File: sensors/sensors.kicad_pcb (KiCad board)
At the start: 2 copper layers, 73 x 56 mm, 84 parts, among them J1 GPIO, J2 JP_CAN, J3 JP_PWM, J4 JP_ADC, J5 JP_GPS, J6 JP_RADIO, SW1 SW_SPDT_321, SW2 SW_SPDT_321, U1 SC16IS752IPW, U2 PCA9685PW, U3 ICM-42605, U4 IST8310, U5 MS5611-01BA, U6 74LVC1G86, U7 ADS1115IDGS, U8 MCP2515-xST, U9 MCP2562-E-MF, Y2 25M-3225, Y4 16MHz

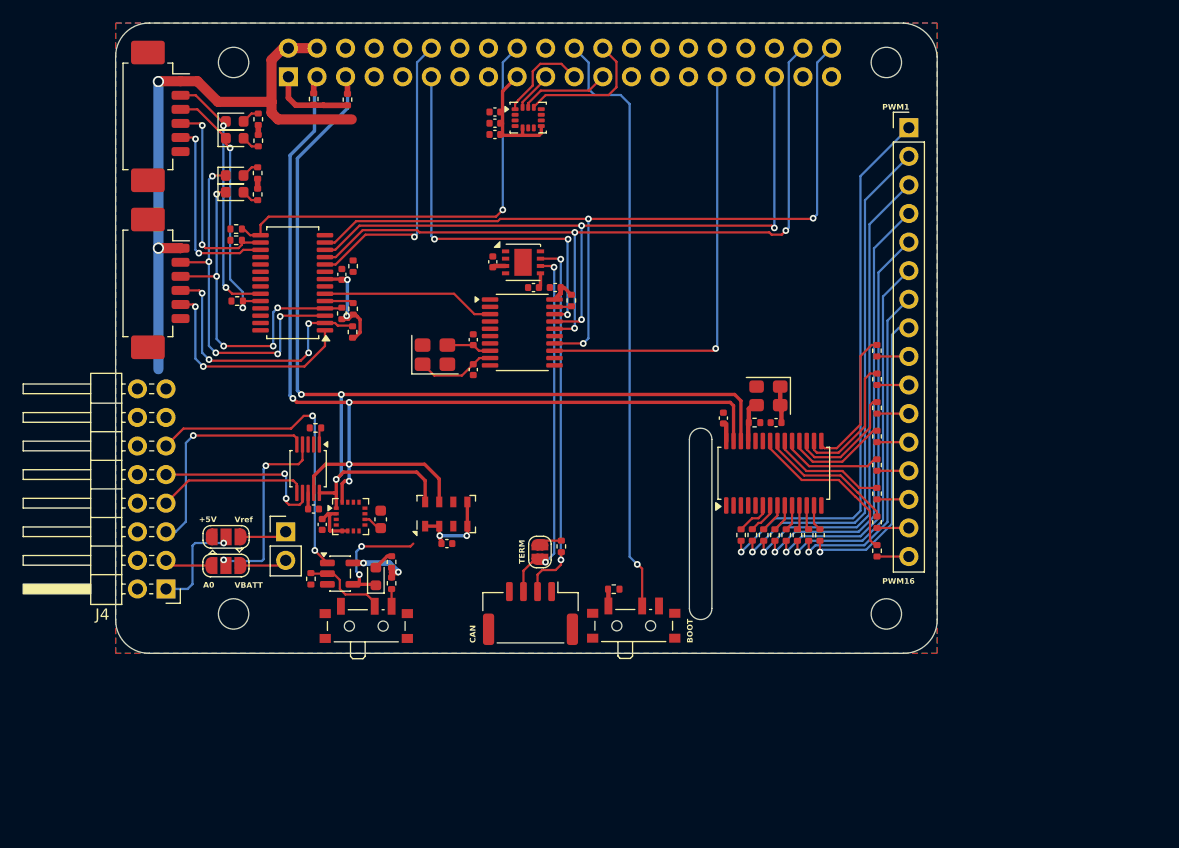
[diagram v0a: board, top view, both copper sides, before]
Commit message: changes from dshot branch
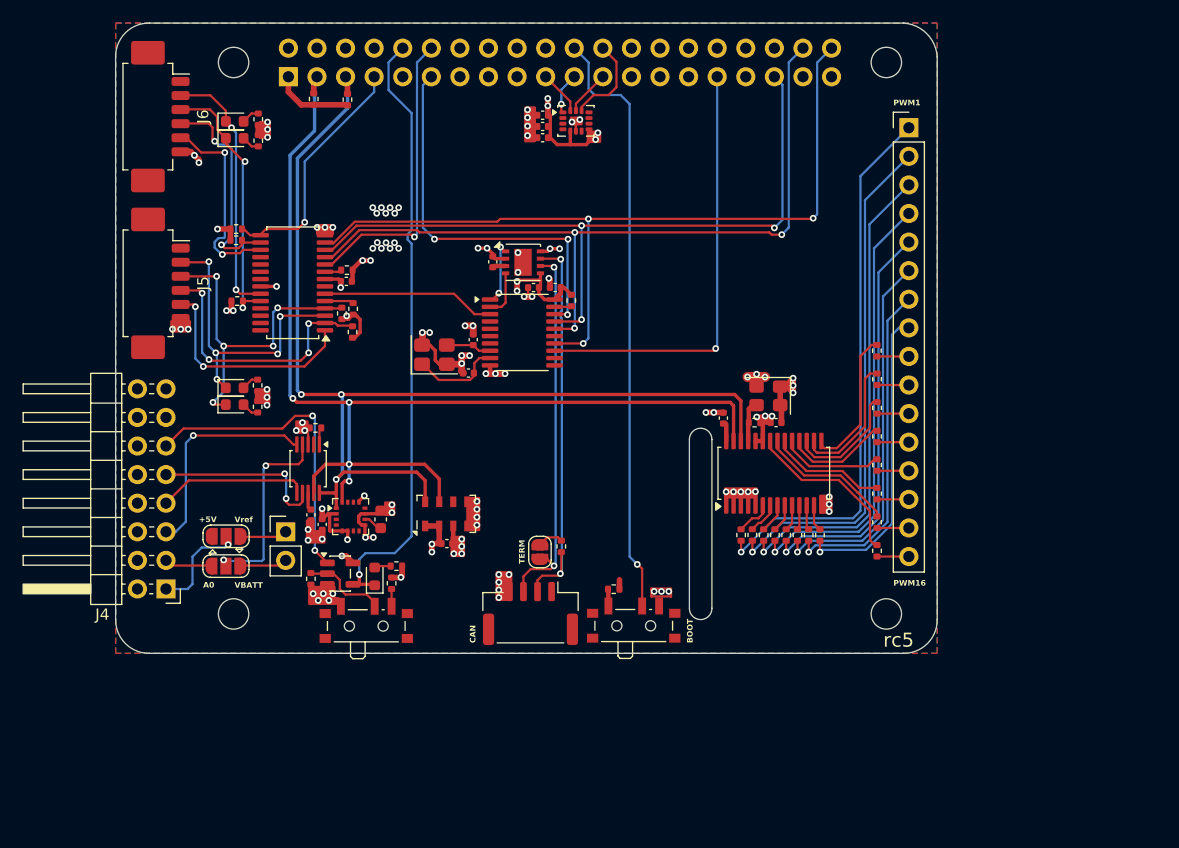
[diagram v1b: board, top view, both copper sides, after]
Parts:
- moved D1 18.9 mm to (110.6, 76.4)
- moved D2 18.9 mm to (110.6, 77.9)
- moved R6 18.9 mm to (112.6, 76.2)
- moved R8 18.9 mm to (112.6, 78.1)
- moved C6 4.25 mm to (137.9, 52.2)
- moved C7 4.25 mm to (137.9, 54.2)
- moved C8 4.25 mm to (137.9, 53.2)
- moved U3 4.25 mm to (140.9, 52.7)
- moved C1 0.74 mm to (120.5, 67.0), turned to 0 degrees
- moved R3 0.65 mm to (120.5, 66.0), turned to 0 degrees
- moved C12 0.57 mm to (117.3, 87.7), turned to -90 degrees
- moved R31 0.57 mm to (125.0, 92.2), turned to 180 degrees
- moved C13 0.52 mm to (131.3, 75.1), turned to 0 degrees
- moved D5 0.10 mm to (123.0, 93.2)
- moved JP1 0.05 mm to (109.8, 89.6)
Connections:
- net /ID_SCL renamed /GPIO1/SCL0
- net /ID_SDA renamed /GPIO0/SDA0
- R2 pad 2: /SDIODAT0/GPIO24 -> /GPIO4/GPCLK0
- U1 pad 15: /SDIODAT0/GPIO24 -> /GPIO4/GPCLK0
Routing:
- net +5V: track 59.0 -> 4.94 mm, vias 2 -> 14
- net GND: track 0.00 -> 47.5 mm, vias 0 -> 79
- net /GPIO15/RXD0: track 10.9 -> 55.3 mm, vias 2 -> 1
- net /SDIODAT0/GPIO24: track 39.8 -> 0.00 mm, vias 1 -> 0
- net /GPIO4/GPCLK0: track 0.00 -> 21.8 mm, vias 0 -> 1
- net +3V3: track 54.3 -> 60.6 mm, vias 6 -> 31
- net /CAN/TXCAN: track 0.00 -> 5.78 mm, vias 0 -> 2
- net /UART/TXA: track 32.8 -> 27.4 mm
- net /GPIO9/SPI0.MISO: track 8.45 -> 3.70 mm, vias 0 -> 1
- net /CAN/RXCAN: track 0.00 -> 4.15 mm
- net /GPIO11/SPI0.SCLK: track 7.97 -> 4.00 mm
- net /GPIO8/SPI0.CE0: track 12.0 -> 8.11 mm
- net /CAN/CANL: track 31.9 -> 33.9 mm
- net /UART/RXA: track 31.5 -> 29.9 mm
- net /CAN/CANH: track 33.6 -> 35.2 mm
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- added copper zone on B.Cu, net +3V3
- added copper zone on F.Cu, net +5V
- added copper zone on In1.Cu, net GND
- added copper zone on In2.Cu, net GND
- removed copper zone on B.Cu, net GND
- removed copper zone on F.Cu, net GND
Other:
- copper layers 2 -> 4
- board text added: "rc5"

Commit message: added 74ACT595 SIPO for DShot bitbanging
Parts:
- added C18: 100nF 10% 16V, Capacitor_SMD:C_0402_1005Metric, F.Cu at (184.8, 94.5)
- added R38: 22Ω ±1%, Resistor_SMD:R_0402_1005Metric, F.Cu at (181.9, 82.5)
- added R39: 22Ω ±1%, Resistor_SMD:R_0402_1005Metric, F.Cu at (181.9, 84.5)
- added R40: 22Ω ±1%, Resistor_SMD:R_0402_1005Metric, F.Cu at (181.9, 86.5)
- added R41: 22Ω ±1%, Resistor_SMD:R_0402_1005Metric, F.Cu at (181.9, 88.5)
- added R42: 22Ω ±1%, Resistor_SMD:R_0402_1005Metric, F.Cu at (181.9, 90.5)
- added R43: 22Ω ±1%, Resistor_SMD:R_0402_1005Metric, F.Cu at (181.9, 92.5)
- added R44: 22Ω ±1%, Resistor_SMD:R_0402_1005Metric, F.Cu at (181.9, 94.5)
- added R45: 22Ω ±1%, Resistor_SMD:R_0402_1005Metric, F.Cu at (181.9, 96.5)
- added U10: 74HCT595, Package_SO:SOP-16_4.4x10.4mm_P1.27mm, F.Cu at (188.1, 87.6)

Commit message: solder pads
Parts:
- removed R31: 470Ω ±1%, Resistor_SMD:R_0402_1005Metric
- added H1: DSHOT1, Connector_Wire:SolderWirePad_1x01_SMD_1x2mm, F.Cu at (173.3, 108.8)
- added H2: DSHOT2, Connector_Wire:SolderWirePad_1x01_SMD_1x2mm, F.Cu at (175.8, 108.8)
- added H3: DSHOT3, Connector_Wire:SolderWirePad_1x01_SMD_1x2mm, F.Cu at (178.4, 108.8)
- added H4: DSHOT4, Connector_Wire:SolderWirePad_1x01_SMD_1x2mm, F.Cu at (180.9, 108.8)
- added H5: DSHOT5, Connector_Wire:SolderWirePad_1x01_SMD_1x2mm, F.Cu at (183.5, 108.8)
- added H6: DSHOT6, Connector_Wire:SolderWirePad_1x01_SMD_1x2mm, F.Cu at (186.0, 108.8)
- added H7: DSHOT7, Connector_Wire:SolderWirePad_1x01_SMD_1x2mm, F.Cu at (188.6, 108.8)
- added H8: DSHOT8, Connector_Wire:SolderWirePad_1x01_SMD_1x2mm, F.Cu at (191.1, 108.8)
- added J6: JP_RADIO, Connector_Molex:Molex_PicoBlade_53261-0671_1x06-1MP_P1.25mm_Horizontal, F.Cu at (103.4, 52.3)
- JP3: footprint Jumper:SolderJumper-2_P1.3mm_Open_RoundedPad1.0x1.5mm -> Connector_PinHeader_2.54mm:PinHeader_1x02_P2.54mm_Vertical
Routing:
- net /CAN/TXCAN: track 5.78 -> 0.00 mm, vias 2 -> 0
- net /CAN/RXCAN: track 4.15 -> 0.00 mm
- net /VREF_OUT: track 8.58 -> 12.0 mm, vias 1 -> 0
- net /CAN/CANL: track 33.9 -> 34.7 mm
- net Net-(U8-OSC1): track 8.03 -> 8.80 mm
- net /CAN/CANH: track 35.2 -> 34.8 mm, vias 2 -> 3

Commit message: solder pads for dshot; resistor layout
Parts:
- removed H1: DSHOT1, Connector_Wire:SolderWirePad_1x01_SMD_1x2mm
- removed H2: DSHOT2, Connector_Wire:SolderWirePad_1x01_SMD_1x2mm
- removed H3: DSHOT3, Connector_Wire:SolderWirePad_1x01_SMD_1x2mm
- removed H4: DSHOT4, Connector_Wire:SolderWirePad_1x01_SMD_1x2mm
- removed H5: DSHOT5, Connector_Wire:SolderWirePad_1x01_SMD_1x2mm
- removed H6: DSHOT6, Connector_Wire:SolderWirePad_1x01_SMD_1x2mm
- removed H7: DSHOT7, Connector_Wire:SolderWirePad_1x01_SMD_1x2mm
- removed H8: DSHOT8, Connector_Wire:SolderWirePad_1x01_SMD_1x2mm
- added J10: DSHOT4, TestPoint:TestPoint_Pad_D1.5mm, F.Cu at (184.4, 112.5)
- added J11: DSHOT5, TestPoint:TestPoint_Pad_D1.5mm, F.Cu at (187.9, 109.0)
- added J12: DSHOT6, TestPoint:TestPoint_Pad_D1.5mm, F.Cu at (187.9, 112.5)
- added J13: DSHOT7, TestPoint:TestPoint_Pad_D1.5mm, F.Cu at (191.5, 109.0)
- added J5: JP_GPS, Connector_Molex:Molex_PicoBlade_53261-0671_1x06-1MP_P1.25mm_Horizontal, F.Cu at (103.4, 67.1)
- added J7: DSHOT1, TestPoint:TestPoint_Pad_D1.5mm, F.Cu at (180.8, 109.0)
- added J8: DSHOT2, TestPoint:TestPoint_Pad_D1.5mm, F.Cu at (180.8, 112.5)
- added J9: DSHOT3, TestPoint:TestPoint_Pad_D1.5mm, F.Cu at (184.4, 109.0)
- moved R38 49.6 mm to (142.7, 112.9), turned to 180 degrees
- moved U10 45.7 mm to (148.1, 109.7), turned to 180 degrees
- moved C18 43.0 mm to (143.2, 105.7), turned to 90 degrees
- moved R39 41.0 mm to (153.6, 114.2)
- moved R40 38.7 mm to (153.6, 112.9)
- moved R41 36.6 mm to (153.6, 111.7)
- moved R42 34.6 mm to (153.6, 110.4)
- moved R43 32.8 mm to (153.6, 109.1)
- moved R44 31.3 mm to (153.6, 107.8)
- moved R45 30.0 mm to (153.6, 106.5)
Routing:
- net +5V: track 4.94 -> 65.9 mm, vias 14 -> 16
- net Net-(U10-QB): track 0.00 -> 1.93 mm
- net Net-(U10-QH): track 0.00 -> 1.92 mm
- net Net-(U10-QC): track 0.00 -> 1.91 mm
- net Net-(U10-QE): track 0.00 -> 1.91 mm
- net Net-(U10-QF): track 0.00 -> 1.91 mm
- net Net-(U10-QD): track 0.00 -> 1.90 mm
- net Net-(U10-QG): track 0.00 -> 1.90 mm

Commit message: lots of changes
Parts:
- added J14: DSHOT8, TestPoint:TestPoint_Pad_D1.5mm, B.Cu at (101.8, 60.3)
- added R31: 470Ω ±1%, Resistor_SMD:R_0402_1005Metric, F.Cu at (125.0, 92.2)
- J10, J11, J12, J13, J7, J8, J9: moved to B.Cu
- JP3: footprint Connector_PinHeader_2.54mm:PinHeader_1x02_P2.54mm_Vertical -> Jumper:SolderJumper-2_P1.3mm_Open_RoundedPad1.0x1.5mm
- U10: value 74HCT595 -> 74AHCT595; footprint Package_SO:SOP-16_4.4x10.4mm_P1.27mm -> pilotpi:WQFN-16-1EP_2.5x3.5mm_P0.5mm
- moved J12 102.7 mm to (101.8, 56.5), turned to -90 degrees
- moved J10 101.9 mm to (101.8, 52.8), turned to -90 degrees
- moved J8 101.4 mm to (101.8, 49.0), turned to -90 degrees
- moved J13 101.0 mm to (104.0, 58.4), turned to -90 degrees
- moved J11 100.0 mm to (104.0, 54.7), turned to -90 degrees
- moved J9 99.3 mm to (103.9, 50.9), turned to -90 degrees
- moved J7 98.7 mm to (103.9, 47.1), turned to -90 degrees
- moved R39 62.6 mm to (128.9, 56.7), turned to -90 degrees
- moved R38 62.0 mm to (129.3, 52.4), turned to -90 degrees
- moved R40 61.0 mm to (129.9, 56.7), turned to -90 degrees
- moved R41 59.5 mm to (130.9, 56.7), turned to -90 degrees
- moved U10 58.2 mm to (132.1, 53.8), turned to 90 degrees
- moved R42 57.9 mm to (131.9, 56.7), turned to -90 degrees
- moved R43 56.4 mm to (132.9, 56.7), turned to -90 degrees
- moved R44 54.8 mm to (133.9, 56.7), turned to -90 degrees
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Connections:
- U10 pad 11: /DShot/CLK -> /GPIO22
- U10 pad 12: /DShot/STR -> /SDIODAT0/GPIO24
- U10 pad 14: /DShot/DAT -> /GPIO23
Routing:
- net +5V: track 65.9 -> 7.66 mm, vias 16 -> 19
- net /DShot/OUT1: track 0.00 -> 37.3 mm, vias 0 -> 1
- net /DShot/OUT8: track 0.00 -> 35.9 mm, vias 0 -> 1
- net /DShot/OUT6: track 0.00 -> 34.8 mm, vias 0 -> 1
- net /DShot/OUT2: track 0.00 -> 34.0 mm, vias 0 -> 1
- net /DShot/OUT7: track 0.00 -> 33.6 mm, vias 0 -> 1
- net /DShot/OUT4: track 0.00 -> 33.1 mm, vias 0 -> 1
- net /DShot/OUT5: track 0.00 -> 32.1 mm, vias 0 -> 1
- net /DShot/OUT3: track 0.00 -> 32.1 mm, vias 0 -> 1
- net /SDIODAT0/GPIO24: track 0.00 -> 8.22 mm
- net /GPIO23: track 0.00 -> 7.35 mm
- net /CAN/TXCAN: track 0.00 -> 5.78 mm, vias 0 -> 2
- net /CAN/RXCAN: track 0.00 -> 4.15 mm
- net /GPIO22: track 0.00 -> 3.96 mm, vias 0 -> 1
- net /VREF_OUT: track 12.0 -> 8.58 mm, vias 0 -> 1
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
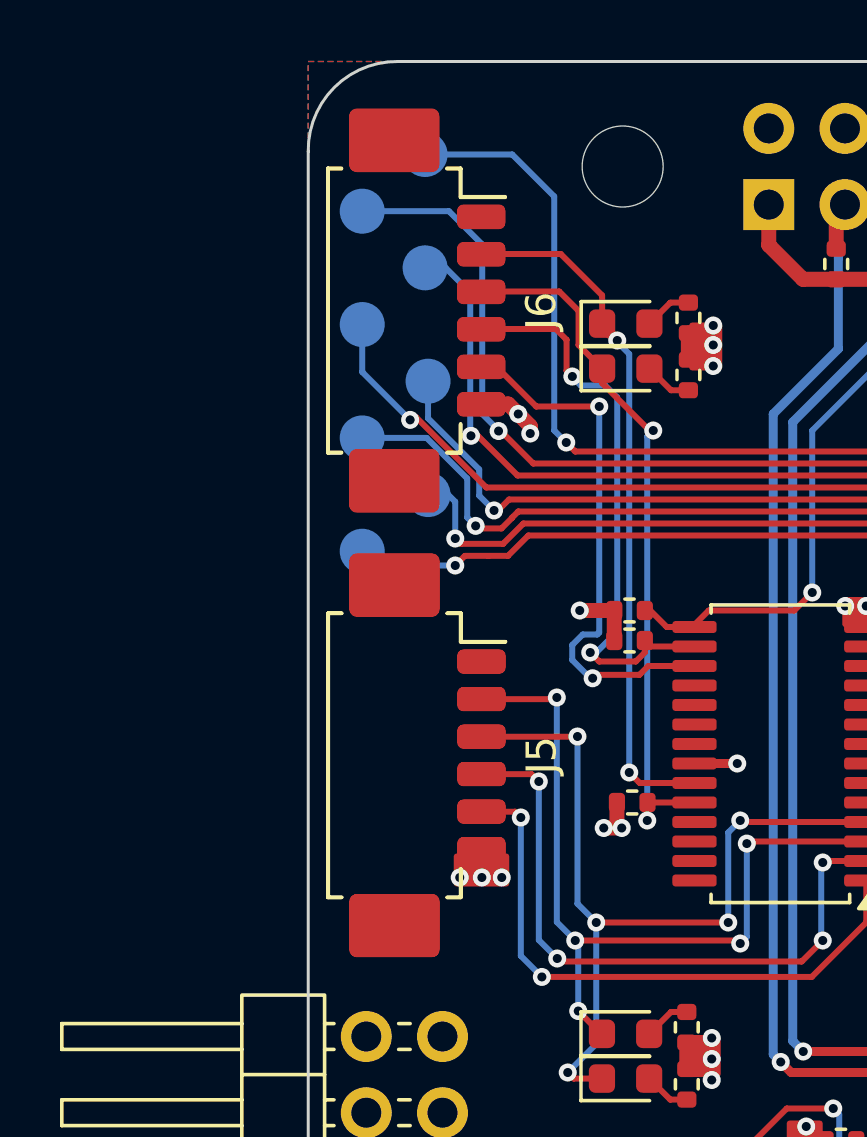
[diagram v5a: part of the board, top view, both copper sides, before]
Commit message: use sheet pins for uart connectors
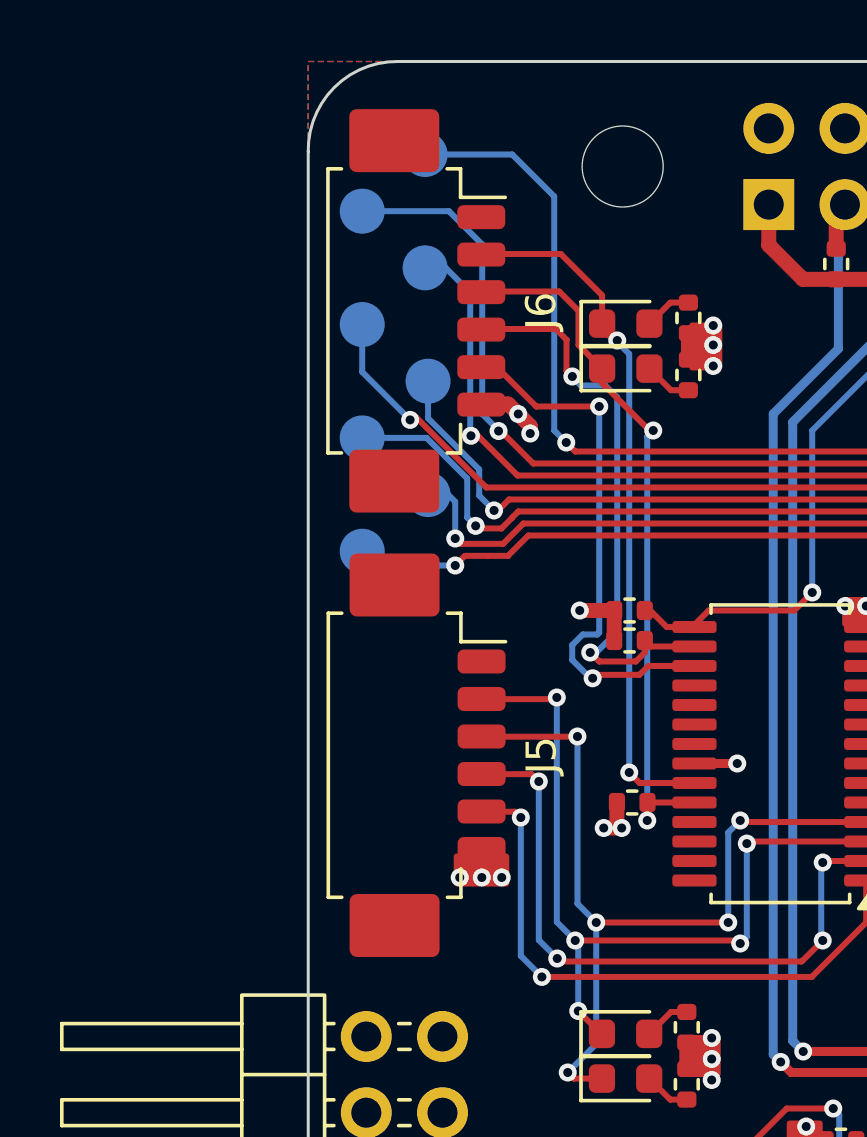
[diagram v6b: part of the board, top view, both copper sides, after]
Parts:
- removed the J5 at (103.4, 67.1)
- removed the J6 at (103.4, 52.3)

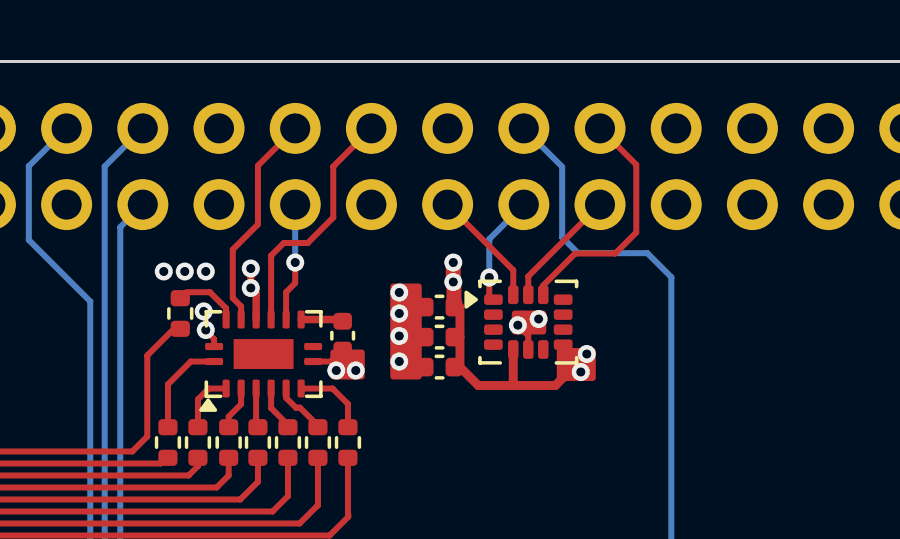
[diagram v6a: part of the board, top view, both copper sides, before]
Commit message: connect SIPO to SPI
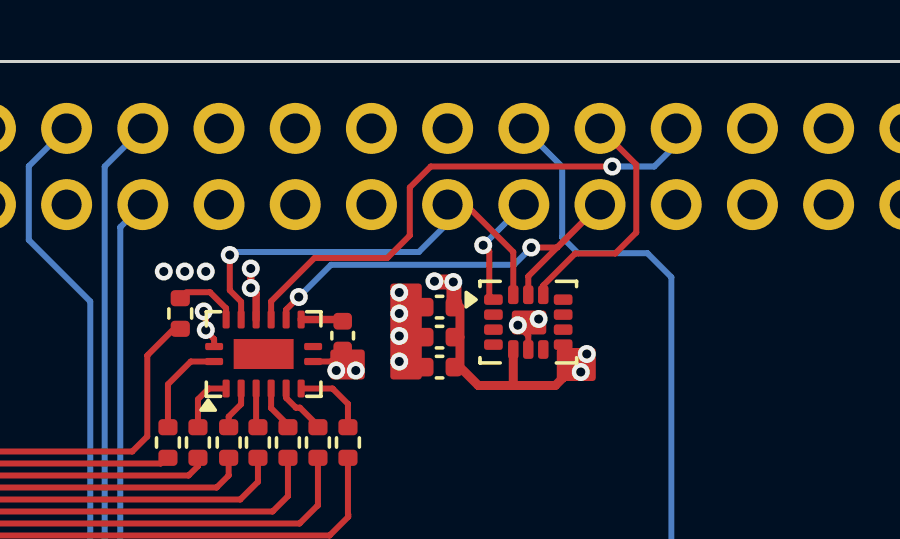
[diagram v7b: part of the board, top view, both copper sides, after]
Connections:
- U10 pad 11: /GPIO22 -> /GPIO11/SPI0.SCLK
- U10 pad 12: /SDIODAT0/GPIO24 -> /GPIO7/SPI0.CE1
- U10 pad 14: /GPIO23 -> /GPIO10/SPI0.MOSI
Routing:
- net /GPIO7/SPI0.CE1: track 0.00 -> 17.8 mm, vias 0 -> 1
- net /GPIO11/SPI0.SCLK: track 4.00 -> 16.2 mm, vias 0 -> 2
- net /GPIO10/SPI0.MOSI: track 3.91 -> 14.9 mm, vias 0 -> 1
- net /SDIODAT0/GPIO24: track 8.22 -> 0.00 mm
- net /GPIO23: track 7.35 -> 0.00 mm
- net /GPIO22: track 3.96 -> 0.00 mm, vias 1 -> 0

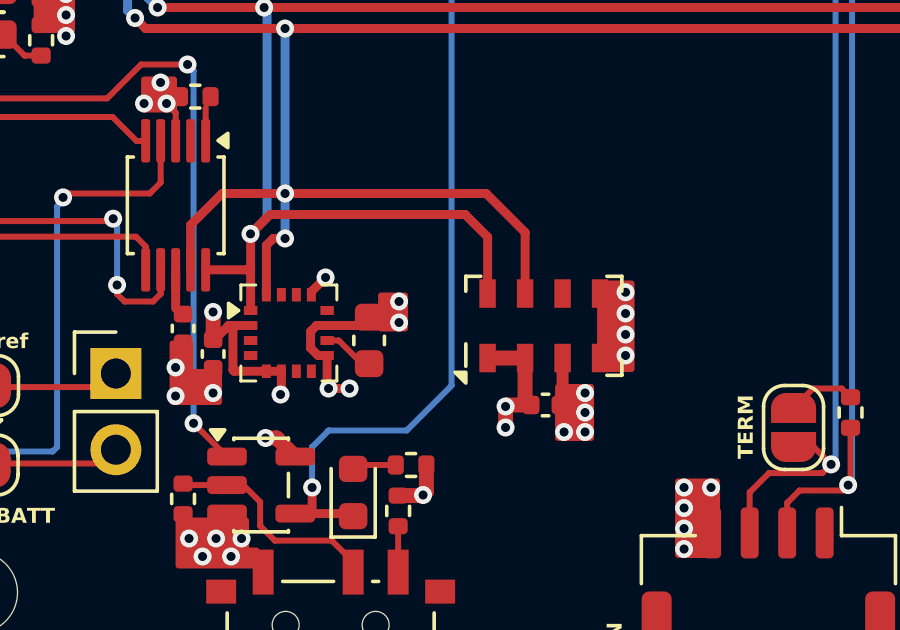
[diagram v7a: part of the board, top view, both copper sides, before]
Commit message: replace MS561101 pressure sensor with SPL06-001
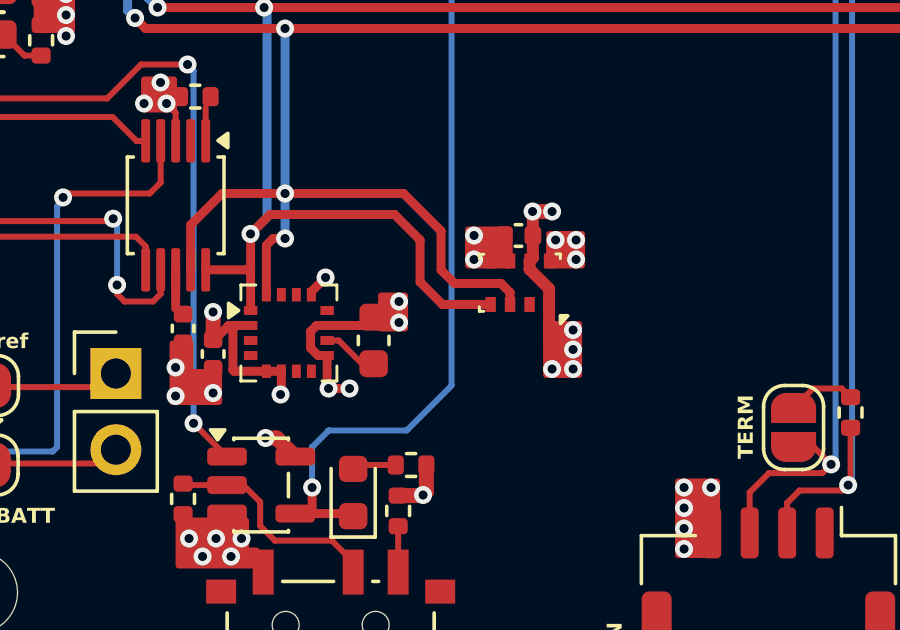
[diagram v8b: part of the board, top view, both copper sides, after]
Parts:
- U5: value MS5611-01BA -> SPL06-001; footprint Package_LGA:LGA-8_3x5mm_P1.25mm -> pilotpi:LGA-8_2.5x2mm_P0.65mm_ClockwisePinNumbering
- moved C11 5.72 mm to (128.5, 84.6)
- moved U5 1.64 mm to (128.6, 86.2), turned to 180 degrees
- moved C10 0.15 mm to (123.7, 88.1)
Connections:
- U5 pad 1: +3V3 -> GND
- U5 pad 2: +3V3 -> unconnected-(U5-CSB-Pad2)
- U5 pad 3: GND -> /GPIO2/SDA1
- U5 pad 4: +3V3 -> /GPIO3/SCL1
- U5 pad 6: unconnected-(U5-SDO-Pad6) -> +3V3
- U5 pad 7: /GPIO2/SDA1 -> GND
- U5 pad 8: /GPIO3/SCL1 -> +3V3
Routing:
- net +3V3: track 60.6 -> 56.2 mm, vias 31 -> 30
- net GND: track 50.4 -> 54.7 mm, vias 83 -> 85
- net /GPIO2/SDA1: track 98.1 -> 97.6 mm
